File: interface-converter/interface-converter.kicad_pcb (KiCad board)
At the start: 2 copper layers, 36.7 x 22.5 mm, 41 parts, among them P1 USB_OTG, P2 CONN_02X05, P3 CONN_02X05, U1 93LCxxB-6, U2 ABM8G-12M, U3 FT232H

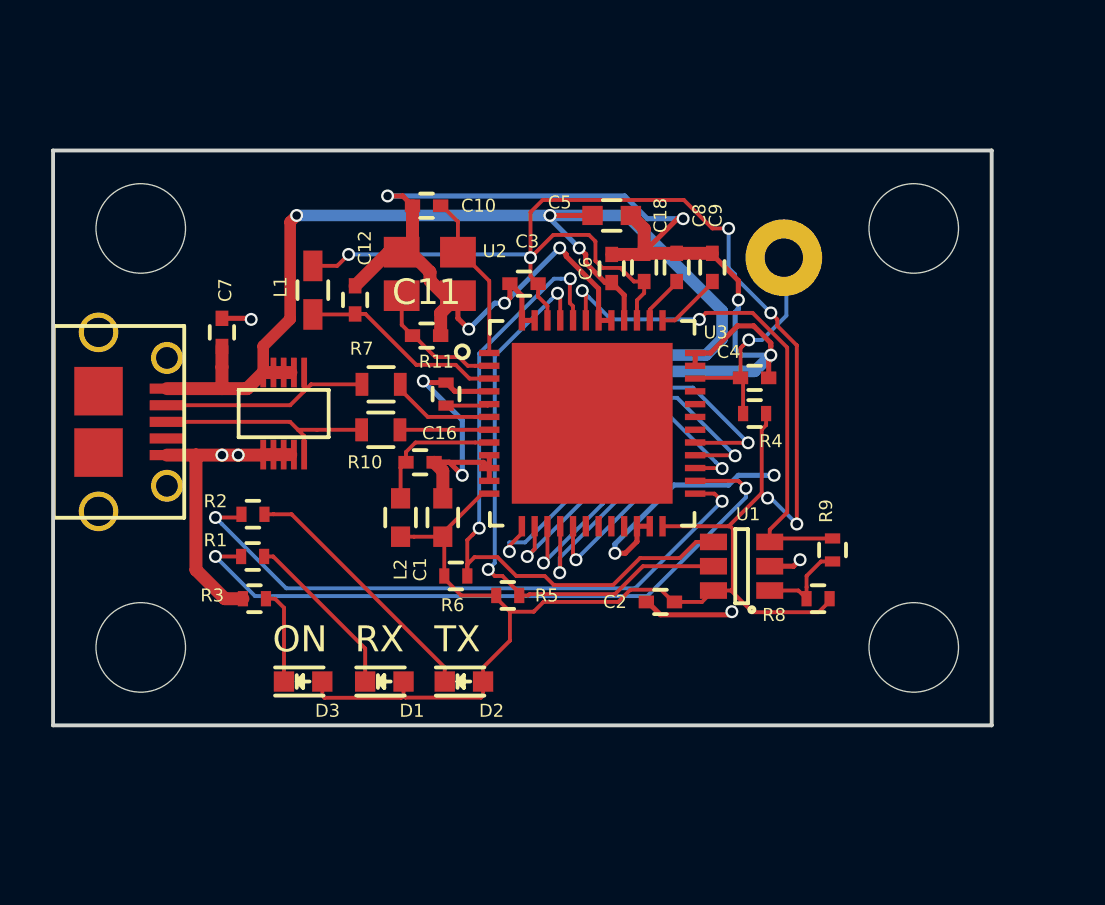
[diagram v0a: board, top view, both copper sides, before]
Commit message: Update of Interface Converter to utilize alternate Power LED
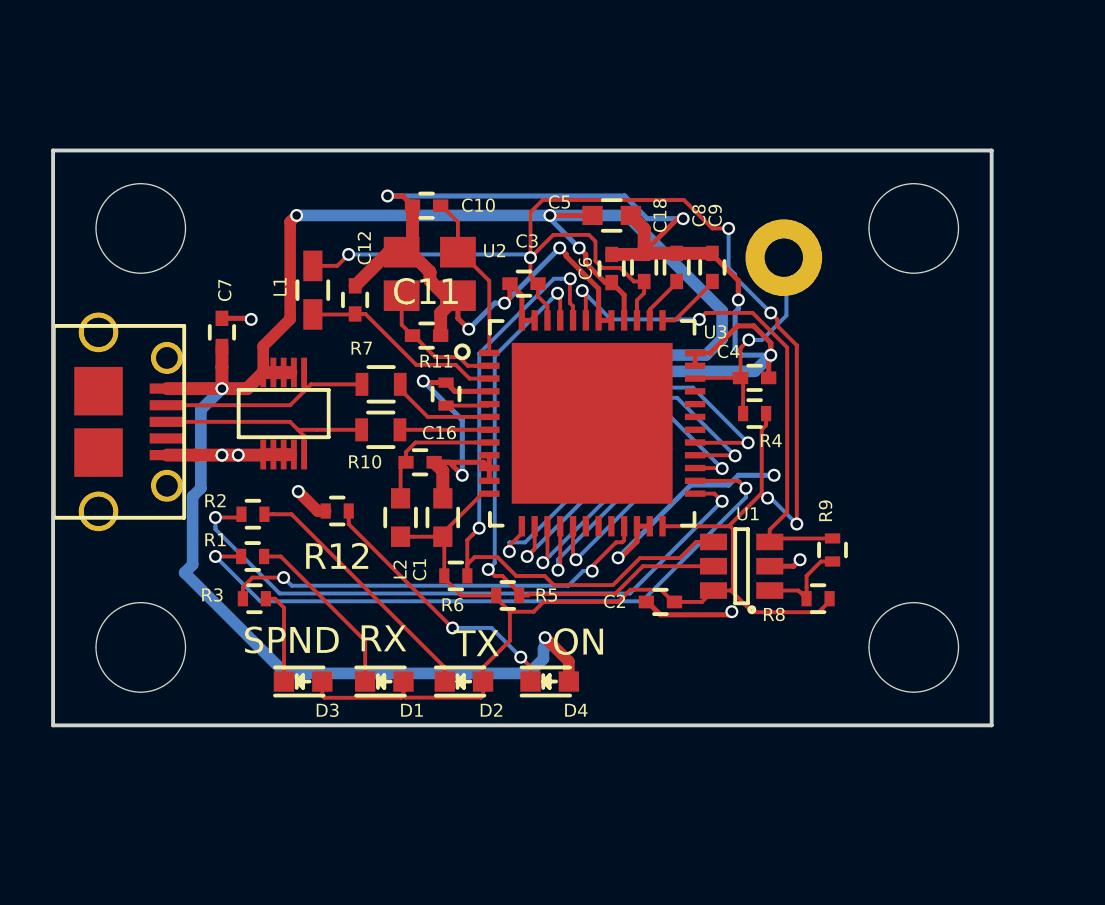
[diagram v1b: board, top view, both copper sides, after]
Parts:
- removed REF** (x4): 1.5mm-spacer, Mounting_Holes:MountingHole_3.5mm
- added D4: LED, LEDs:LED_0603, F.Cu at (129.3, 138.7)
- added P4: CONN_01X01, Mounting_Holes:MountingHole_3.5mm, F.Cu at (143.5, 121.0)
- added P5: CONN_01X01, Mounting_Holes:MountingHole_3.5mm, F.Cu at (113.3, 137.4)
- added P6: CONN_01X01, Mounting_Holes:MountingHole_3.5mm, F.Cu at (143.5, 137.4)
- added P7: CONN_01X01, Mounting_Holes:MountingHole_3.5mm, F.Cu at (113.3, 121.0)
- added R12: 150, Resistors_SMD:R_0402, F.Cu at (121.0, 132.1)
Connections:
- R3 pad 2: GND -> /AC0
- U3 pad 21: (no net) -> /AC0
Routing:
- net /Vbus: track 52.8 -> 79.5 mm, vias 3 -> 5
- net /AC0: track 0.00 -> 17.0 mm, vias 0 -> 2
- net Net-(D4-Pad1): track 0.00 -> 10.5 mm, vias 0 -> 2
- net GND: track 105.6 -> 99.9 mm, vias 16 -> 17
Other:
- board text added: "SPND"

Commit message: Huge slew of changes for 3D parts, addition of BNO adapter and digital isolator adapter
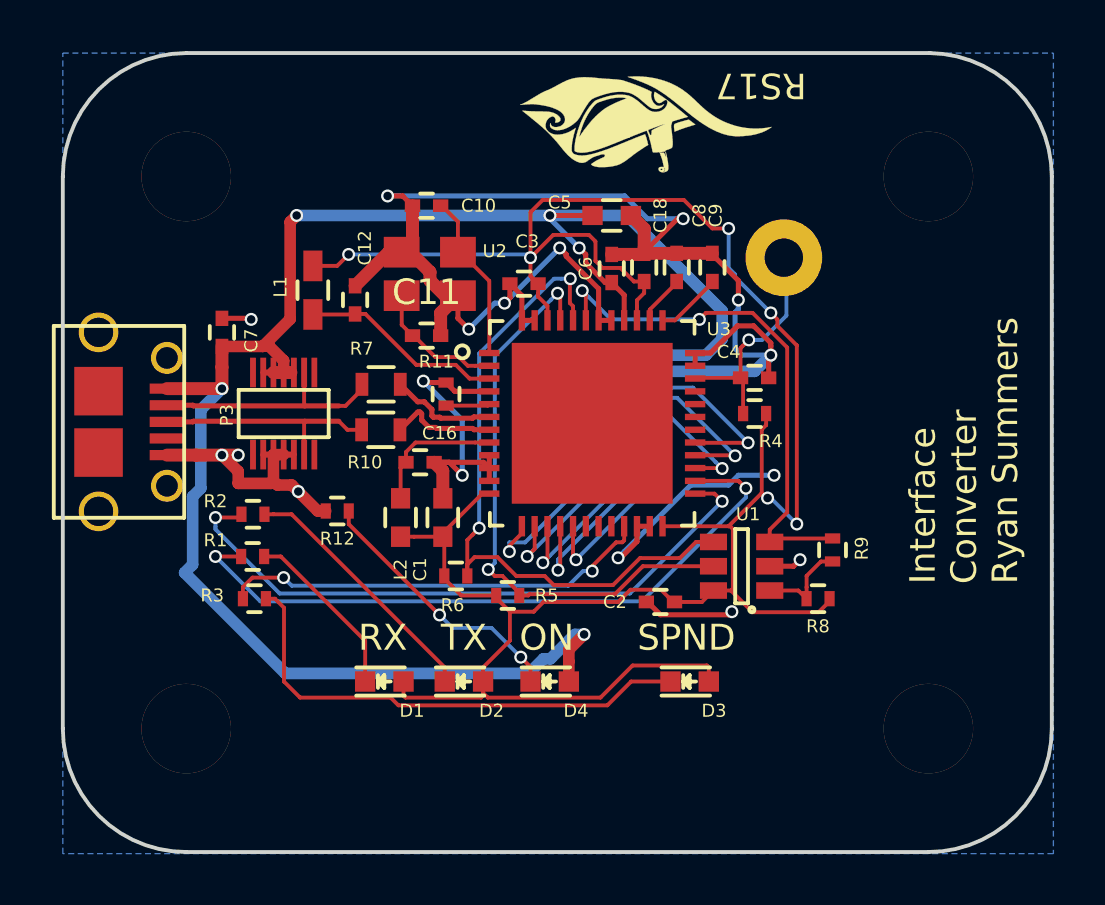
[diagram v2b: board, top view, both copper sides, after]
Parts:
- added G***: LOGO, robosub_footprints:robosub_logo-medium, F.Cu at (133.0, 116.8)
- P4, P5, P6, P7: footprint Mounting_Holes:MountingHole_3.5mm -> robosub_footprints:1.5mm-spacer
- moved D3 15.1 mm to (134.7, 138.7)
- moved P5 3.64 mm to (115.1, 140.6)
- moved P6 3.23 mm to (144.1, 140.6)
- moved P7 2.70 mm to (115.1, 119.0)
- moved P4 2.11 mm to (144.1, 119.0)
- moved P2 0.06 mm to (131.3, 128.1)
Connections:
- net Net-(R10-Pad1) renamed /usb_f+
- net Net-(R7-Pad1) renamed /usb_f-
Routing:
- net Net-(D3-Pad1): track 3.74 -> 19.6 mm
- net +3V3: track 88.3 -> 94.5 mm
- net GND: track 99.9 -> 102.3 mm
- net /usb_f+: track 3.49 -> 4.21 mm
- net /USB-: track 8.69 -> 9.41 mm
- net /Vbus: track 79.5 -> 80.1 mm
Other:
- board size 36.7 x 22.5 mm -> 38.7 x 31.2 mm
- net class PWR: trace_width 0.454 -> 0.2388
- board text added: "Interface Converter Ryan Summers"
- board text added: "RS17"

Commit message: Modified USB routing and isolated ground from the clock signal
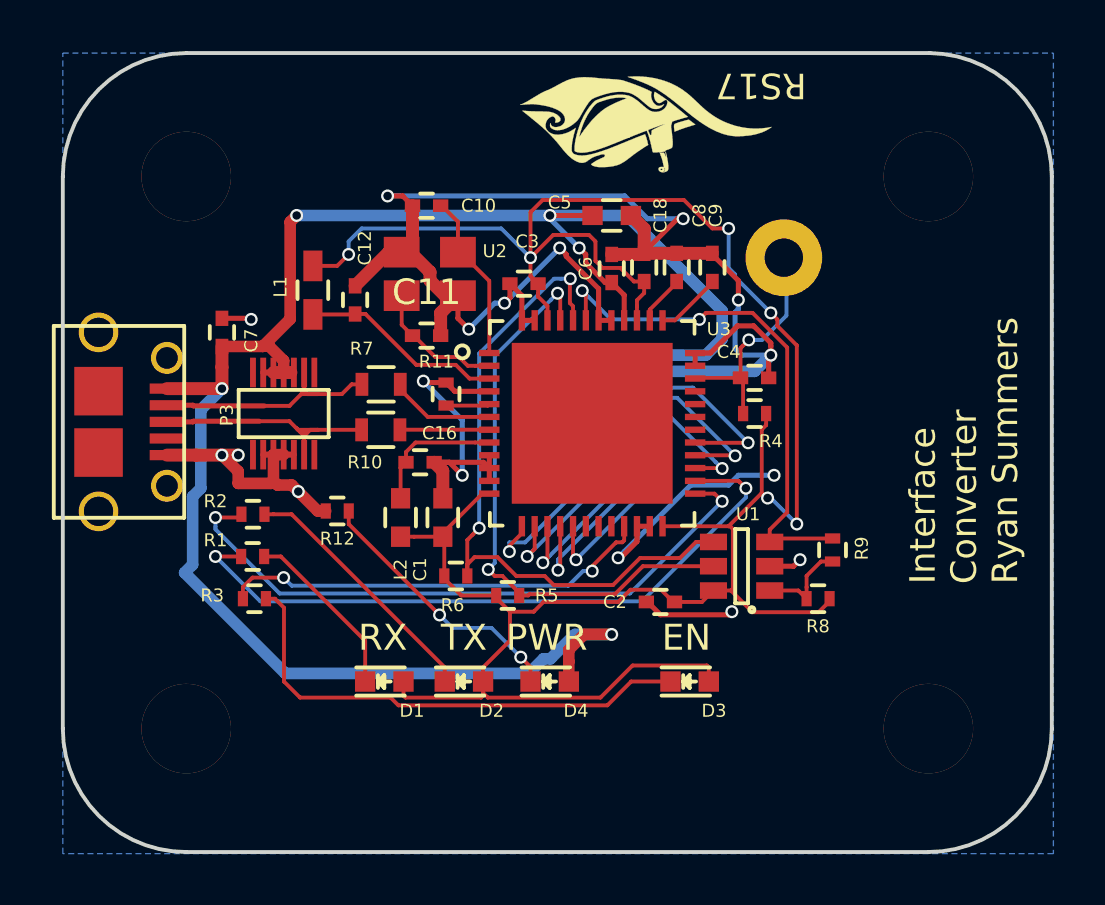
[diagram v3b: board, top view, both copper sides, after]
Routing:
- net /Vbus: track 80.1 -> 83.2 mm
- net GND: track 102.3 -> 104.1 mm
- net +3V3: track 94.5 -> 95.8 mm
- net /USB+: track 9.08 -> 9.84 mm
- net /usb_f+: track 4.21 -> 3.49 mm
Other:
- board text added: "EN"
- board text added: "PWR"
- board text removed: "ON"
- board text removed: "SPND"

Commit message: Update to include test points for FTDI signals
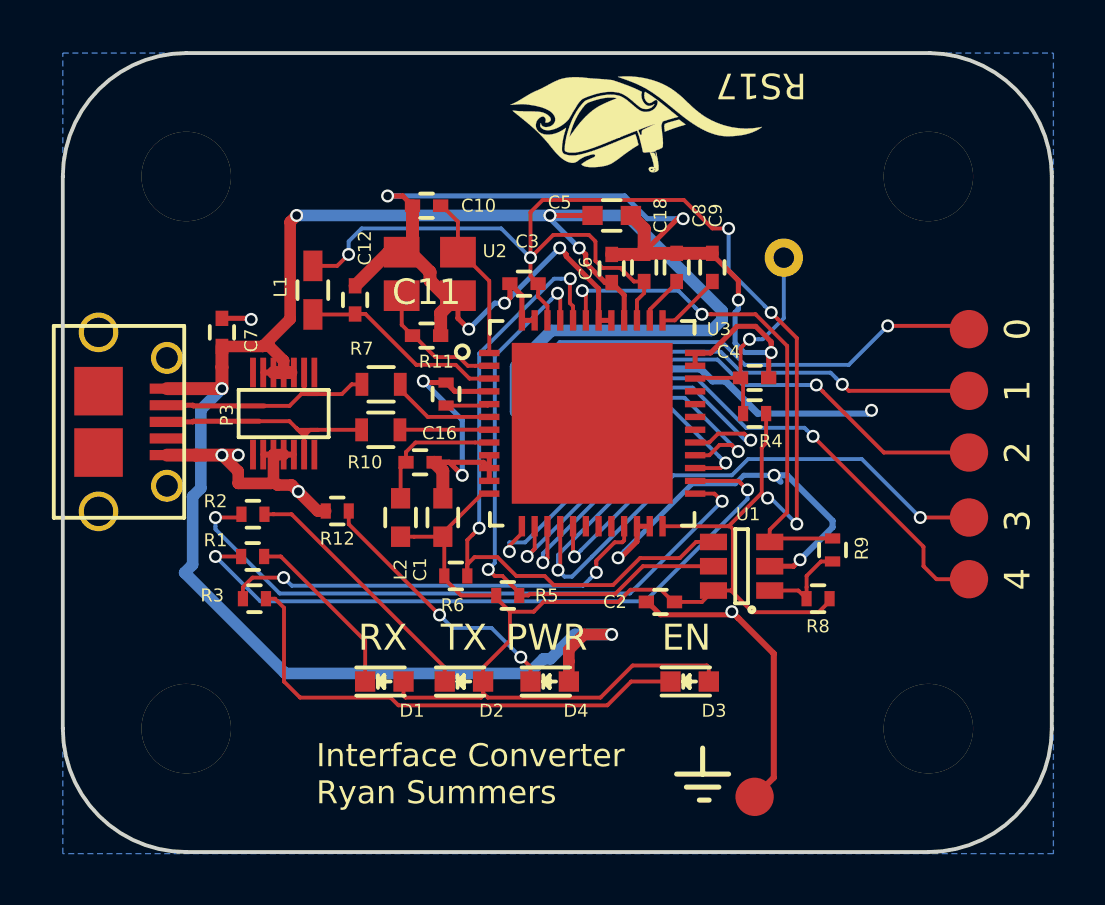
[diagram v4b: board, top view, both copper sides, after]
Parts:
- added P10: TST, Measurement_Points:Measurement_Point_Round-SMD-Pad_Small, F.Cu at (145.7, 129.8)
- added P11: TST, Measurement_Points:Measurement_Point_Round-SMD-Pad_Small, F.Cu at (145.7, 127.4)
- added P12: TST, Measurement_Points:Measurement_Point_Round-SMD-Pad_Small, F.Cu at (145.7, 125.0)
- added P13: TST, Measurement_Points:Measurement_Point_Round-SMD-Pad_Small, F.Cu at (137.3, 143.3)
- added P8: TST, Measurement_Points:Measurement_Point_Round-SMD-Pad_Small, F.Cu at (145.7, 134.7)
- added P9: TST, Measurement_Points:Measurement_Point_Round-SMD-Pad_Small, F.Cu at (145.7, 132.3)
- W1: footprint Measurement_Points:Measurement_Point_Round-TH_Big -> Measurement_Points:Measurement_Point_Round-TH_Small
- moved G*** 0.38 mm to (132.6, 116.8)
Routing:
- net GND: track 104.1 -> 128.1 mm, vias 17 -> 18
- net /AD0: track 8.86 -> 30.5 mm, vias 1 -> 2
- net /AD1: track 9.19 -> 29.3 mm, vias 1 -> 2
- net /AD2: track 10.1 -> 30.1 mm, vias 1 -> 2
- net /AD4: track 9.10 -> 28.7 mm, vias 1 -> 2
- net /AD3: track 8.52 -> 27.5 mm, vias 1 -> 2
- net /Vbus: track 83.2 -> 84.0 mm
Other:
- net class PWR: trace_width 0.2388 -> 0.2788
- board text added: "0"
- board text added: "1"
- board text added: "2"
- board text added: "3"
- board text added: "4"
